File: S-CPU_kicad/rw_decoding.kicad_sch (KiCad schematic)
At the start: 134 parts

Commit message: Schematics tidying in progress.
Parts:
- added GBEG: OR_3, symbol Ricoh_Cells:OR_3
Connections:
- net MODE2_OR_MODE3: now also GBEG.3
- net RW_EN: now also GBEG.4
- net SYNCED_REFRESH_EN: now also GBEG.1
- new net ~{INTERNAL_CYCLE}: GBEG.2
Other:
- company: (none) -> Author: Regis Galland
- title: (none) -> SNES S-CPU Schematics 
- moved on the sheet: AABC, AAFD, BAAG, BABW, BAEH, BAGU, BAIS, BALC, BASL, BATZ, BAUV, CACL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

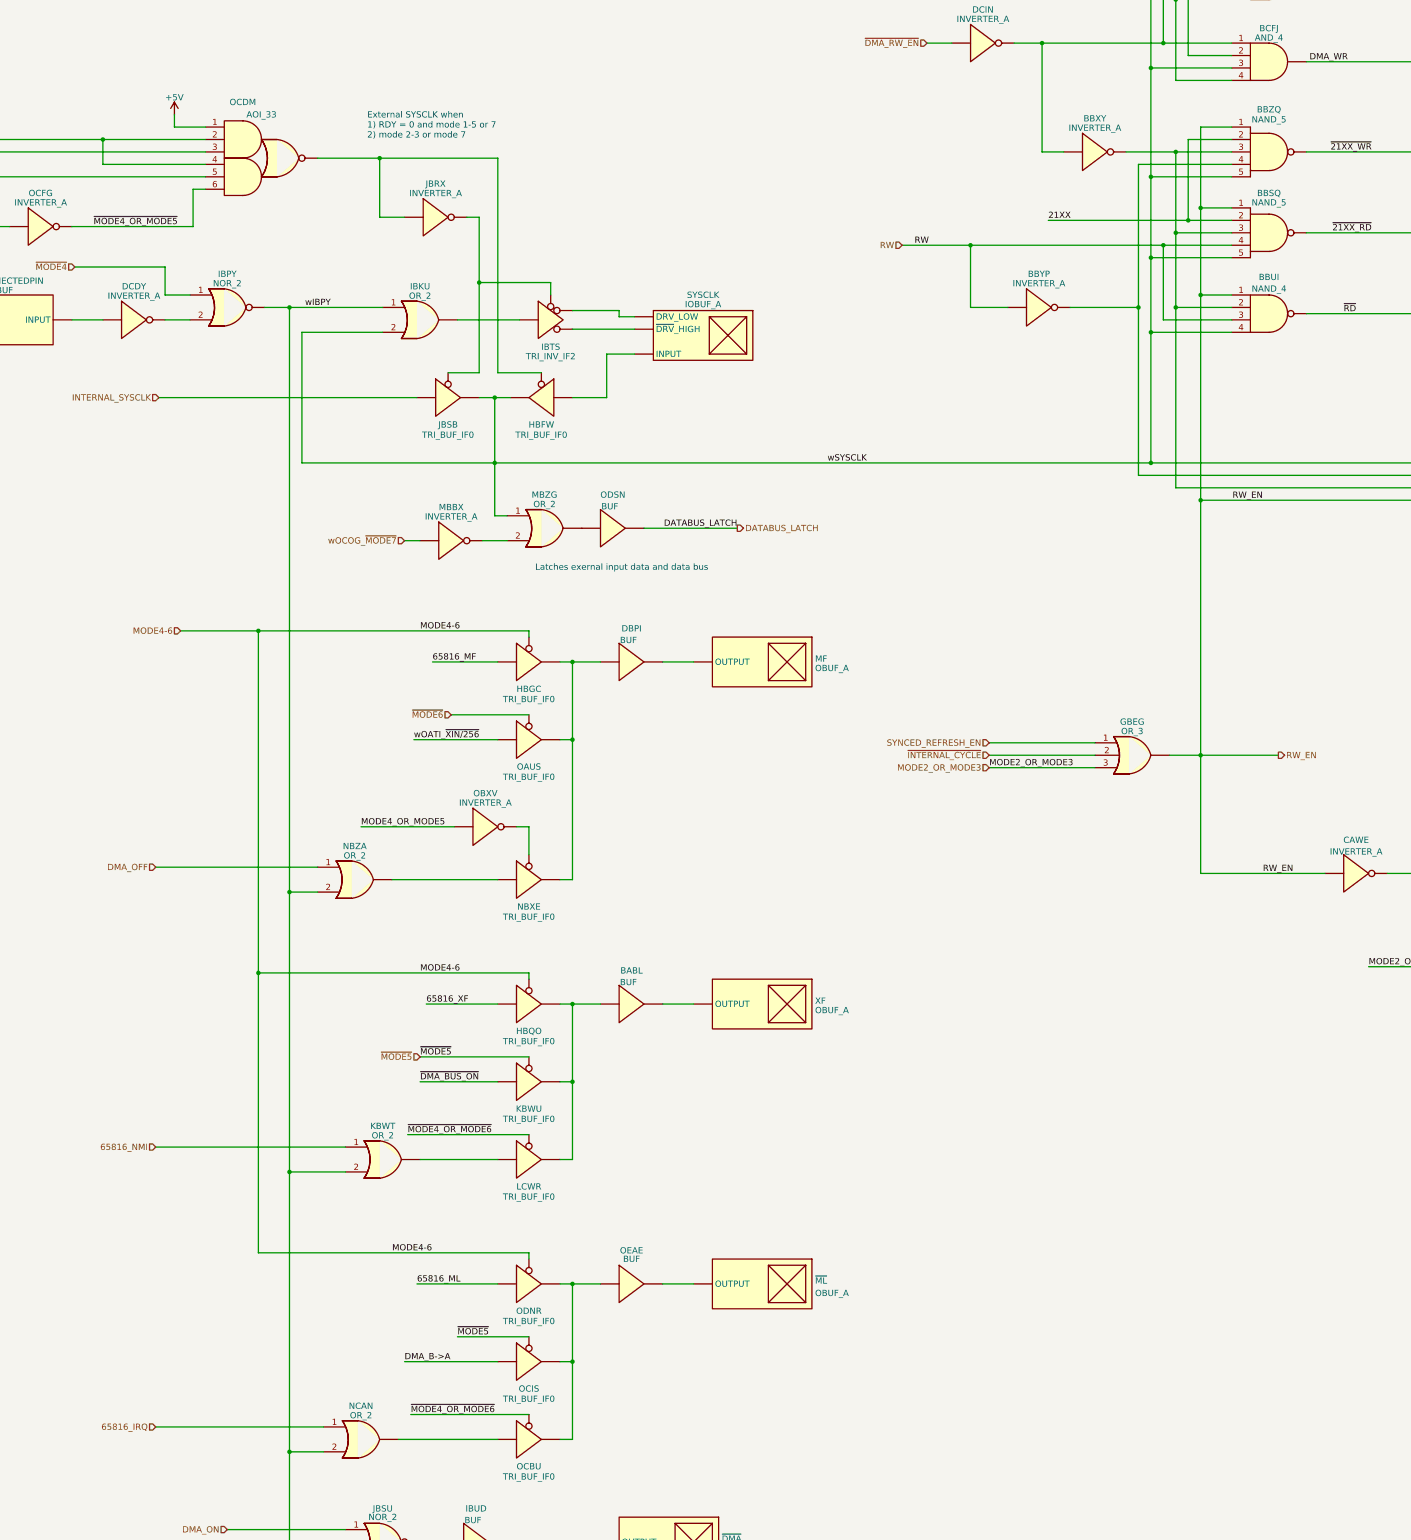
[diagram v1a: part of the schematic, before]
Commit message: Big update on the hierarchical sheet. DMA section update too.
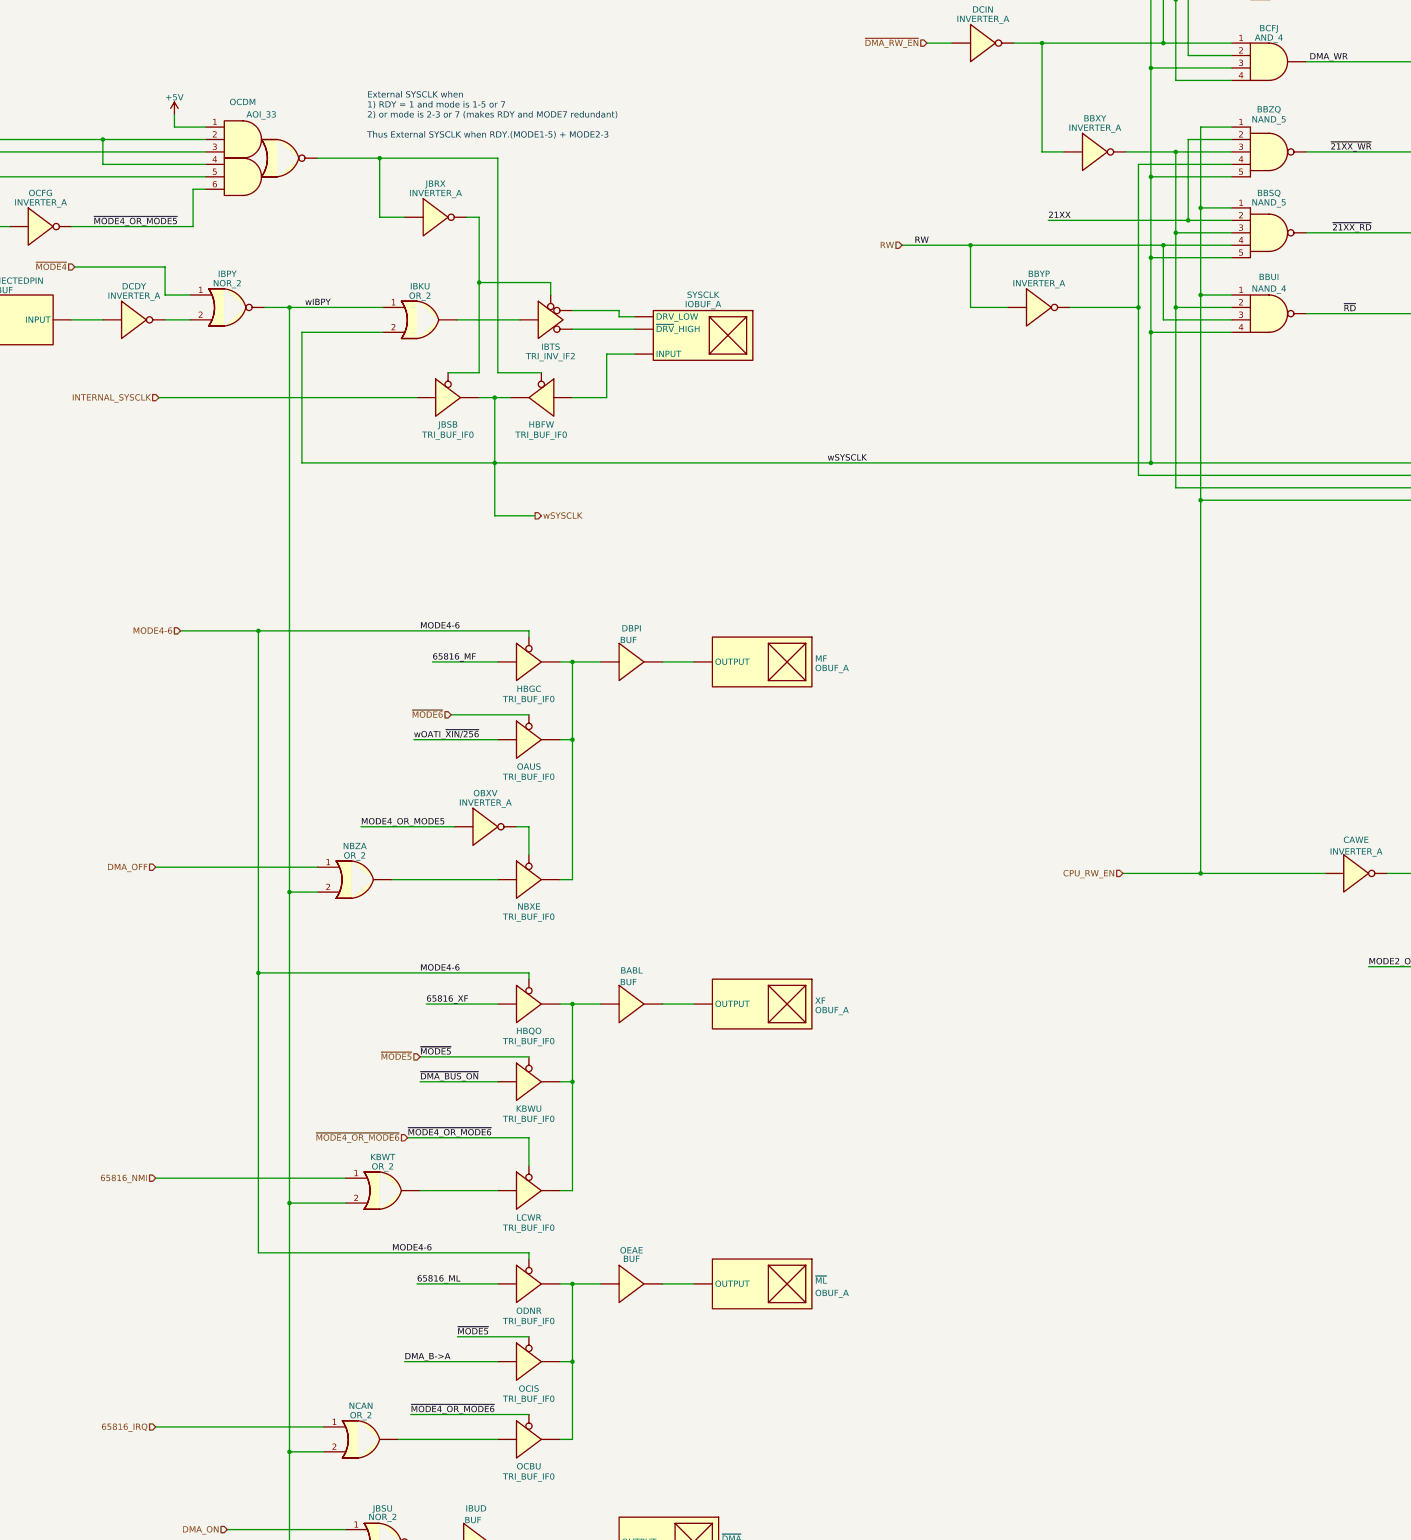
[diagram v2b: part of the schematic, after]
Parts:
- removed GBEG: OR_3, symbol Ricoh_Cells:OR_3
- removed MBBX: INVERTER_A, symbol Ricoh_Cells:INVERTER_A
- removed MBZG: OR_2, symbol Ricoh_Cells:OR_2
- removed ODSN: BUF, symbol Ricoh_Cells:BUF
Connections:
- net RW_EN renamed CPU_RW_EN
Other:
- note added: "External SYSCLK when 1) RDY = 1 and mode is 1-5 or 7 2) or mode is 2-3 or 7 (makes RDY and MODE7 redundant) Thus External SYSCLK when RDY.(MODE1-5) + MODE2-3"
- note removed: "External SYSCLK when 1) RDY = 0 and mode 1-5 or 7 2) mode 2-3 or mode 7"
- note removed: "Latches exernal input data and data bus"
- moved on the sheet: KBWT, LCWR

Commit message: DMA section update. Found errors between some MUX and MUXI gates.
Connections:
- net RW renamed R~{W}
- net ~{DMA_BUS_ON} renamed HDMA_TABLE_RD
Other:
- note added: "Internal registers only In NES mode (MODE2-3), only 4016 and 4017 will set CPU_REG_RD to 1."
- note removed: "Internal registers only"
- moved on the sheet: BBXY, BBYP
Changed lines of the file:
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@@
   (junction (at 533.4 466.725) (diameter 0) (color 0 0 0 0)
   )
-  (junction (at 363.855 187.96) (diameter 0) (color 0 0 0 0)
-  )
   (junction (at 371.475 172.72) (diameter 0) (color 0 0 0 0)
   )
@@
   (junction (at 344.17 133.985) (diameter 0) (color 0 0 0 0)
   )
+  (junction (at 363.855 158.75) (diameter 0) (color 0 0 0 0)
+  )
   (junction (at 229.235 182.88) (diameter 0) (color 0 0 0 0)
   )
@@
   )
   (junction (at 521.335 441.96) (diameter 0) (color 0 0 0 0)
-  )
-  (junction (at 376.555 303.53) (diameter 0) (color 0 0 0 0)
   )
   (no_connect (at 436.245 202.565))
@@
     (stroke (width 0) (type default))
   )
-  (wire (pts (xy 363.855 187.96) (xy 363.855 158.75))
-    (stroke (width 0) (type default))
-  )
   (wire (pts (xy 561.34 330.2) (xy 568.325 330.2))
     (stroke (width 0) (type default))
@@
     (stroke (width 0) (type default))
   )
-  (wire (pts (xy 376.555 303.53) (xy 401.955 303.53))
+  (wire (pts (xy 395.605 303.53) (xy 401.955 303.53))
     (stroke (width 0) (type default))
   )
@@
     (stroke (width 0) (type default))
   )
-  (wire (pts (xy 329.565 187.96) (xy 337.185 187.96))
+  (wire (pts (xy 329.565 158.75) (xy 334.01 158.75))
     (stroke (width 0) (type default))
   )
@@
     (stroke (width 0) (type default))
   )
-  (wire (pts (xy 349.885 187.96) (xy 363.855 187.96))
+  (wire (pts (xy 346.71 158.75) (xy 363.855 158.75))
     (stroke (width 0) (type default))
   )
@@
     (stroke (width 0) (type default))
   )
-  (wire (pts (xy 363.855 187.96) (xy 363.855 222.25))
+  (wire (pts (xy 363.855 158.75) (xy 363.855 222.25))
     (stroke (width 0) (type default))
   )
@@
     (stroke (width 0) (type default))
   )
-  (wire (pts (xy 361.315 156.21) (xy 371.475 156.21))
+  (wire (pts (xy 361.315 146.05) (xy 371.475 146.05))
     (stroke (width 0) (type default))
   )
@@
     (stroke (width 0) (type default))
   )
-  (wire (pts (xy 376.555 227.33) (xy 376.555 303.53))
-    (stroke (width 0) (type default))
-  )
   (wire (pts (xy 532.765 132.715) (xy 530.225 132.715))
     (stroke (width 0) (type default))
@@
     (stroke (width 0) (type default))
   )
-  (wire (pts (xy 344.17 156.21) (xy 344.17 133.985))
+  (wire (pts (xy 344.17 146.05) (xy 344.17 133.985))
     (stroke (width 0) (type default))
   )
@@
     (stroke (width 0) (type default))
   )
+  (wire (pts (xy 371.475 146.05) (xy 371.475 156.21))
+    (stroke (width 0) (type default))
+  )
   (wire (pts (xy 468.63 394.335) (xy 476.25 394.335))
     (stroke (width 0) (type default))
@@
     (stroke (width 0) (type default))
   )
-  (wire (pts (xy 344.17 156.21) (xy 348.615 156.21))
+  (wire (pts (xy 344.17 146.05) (xy 348.615 146.05))
     (stroke (width 0) (type default))
   )
@@
     (stroke (width 0) (type default))
   )
-  (wire (pts (xy 329.565 175.26) (xy 329.565 187.96))
+  (wire (pts (xy 329.565 158.75) (xy 329.565 175.26))
     (stroke (width 0) (type default))
   )
@@
     (stroke (width 0) (type default))
   )
-  (wire (pts (xy 376.555 303.53) (xy 360.68 303.53))
+  (wire (pts (xy 376.555 227.33) (xy 358.775 227.33))
     (stroke (width 0) (type default))
   )
@@
     (effects (font (size 5 5) (thickness 1) bold) (justify left bottom))
   )
-  (text "Internal registers only" (at 631.825 318.77 0)
+  (text "Internal registers only\nIn NES mode (MODE2-3), only 4016 and 4017\nwill set CPU_REG_RD to 1. "
+    (at 617.855 329.565 0)
     (effects (font (size 1.27 1.27)) (justify left bottom))
   )
@@
     (effects (font (size 1.27 1.27)) (justify left bottom))
   )
-  (label "RW" (at 318.135 175.26 0) (fields_autoplaced)
+  (label "R~{W}" (at 318.135 175.26 0) (fields_autoplaced)
     (effects (font (size 1.27 1.27)) (justify left bottom))
   )
@@
     (effects (font (size 1.27 1.27)) (justify left bottom))
   )
-  (label "~{DMA_BUS_ON}" (at 317.5 87.63 0) (fields_autoplaced)
+  (label "HDMA_TABLE_RD" (at 317.5 87.63 0) (fields_autoplaced)
     (effects (font (size 1.27 1.27)) (justify left bottom))
   )
@@
     (effects (font (size 1.27 1.27)) (justify right bottom))
   )
-  (label "~{DMA_BUS_ON}" (at 217.17 346.075 0) (fields_autoplaced)
+  (label "HDMA_TABLE_RD" (at 217.17 346.075 0) (fields_autoplaced)
     (effects (font (size 1.27 1.27)) (justify left bottom))
   )
@@
     (effects (font (size 1.27 1.27)) (justify right))
   )
+  (hierarchical_label "CPU_RW_EN" (shape input) (at 395.605 303.53 180) (fields_autoplaced)
+    (effects (font (size 1.27 1.27)) (justify right))
+  )
   (hierarchical_label "~{MODE1}" (shape input) (at 128.27 161.29 180) (fields_autoplaced)
     (effects (font (size 1.27 1.27)) (justify right))
@@
     (effects (font (size 1.27 1.27)) (justify right))
   )
-  (hierarchical_label "RW" (shape input) (at 315.595 175.26 180) (fields_autoplaced)
+  (hierarchical_label "R~{W}" (shape input) (at 315.595 175.26 180) (fields_autoplaced)
     (effects (font (size 1.27 1.27)) (justify right))
   )
@@
     (effects (font (size 1.27 1.27)) (justify right))
   )
-  (hierarchical_label "CPU_RW_EN" (shape input) (at 360.68 303.53 180) (fields_autoplaced)
+  (hierarchical_label "CPU_RW_EN" (shape input) (at 358.775 227.33 180) (fields_autoplaced)
     (effects (font (size 1.27 1.27)) (justify right))
   )
@@
     (effects (font (size 1.27 1.27)) (justify left))
   )
-  (hierarchical_label "~{DMA_BUS_ON}" (shape input) (at 317.5 87.63 180) (fields_autoplaced)
+  (hierarchical_label "HDMA_TABLE_RD" (shape input) (at 317.5 87.63 180) (fields_autoplaced)
     (effects (font (size 1.27 1.27)) (justify right))
   )
@@
     )
   )
-  (symbol (lib_id "Ricoh_Cells:INVERTER_A") (at 354.965 156.21 0) (unit 1)
+  (symbol (lib_id "Ricoh_Cells:INVERTER_A") (at 354.965 146.05 0) (unit 1)
     (in_bom yes) (on_board yes) (dnp no) (fields_autoplaced)
-    (property "Reference" "BBXY" (at 354.965 149.3901 0)
-      (effects (font (size 1.27 1.27)))
-    )
-    (property "Value" "INVERTER_A" (at 354.965 151.3111 0)
-      (effects (font (size 1.27 1.27)))
-    )
-    (property "Footprint" "" (at 352.425 156.21 0)
-      (effects (font (size 1.27 1.27)) hide)
-    )
-    (property "Datasheet" "http://iceboy.a-singer.de/doc/dmg_cells.html#inv_a" (at 356.235 163.83 0)
+    (property "Reference" "BBXY" (at 354.965 139.2301 0)
+      (effects (font (size 1.27 1.27)))
+    )
+    (property "Value" "INVERTER_A" (at 354.965 141.1511 0)
+      (effects (font (size 1.27 1.27)))
+    )
+    (property "Footprint" "" (at 352.425 146.05 0)
+      (effects (font (size 1.27 1.27)) hide)
+    )
+    (property "Datasheet" "http://iceboy.a-singer.de/doc/dmg_cells.html#inv_a" (at 356.235 153.67 0)
       (effects (font (size 1.27 1.27)) hide)
     )
@@
     )
   )
-  (symbol (lib_id "Ricoh_Cells:INVERTER_A") (at 343.535 187.96 0) (unit 1)
+  (symbol (lib_id "Ricoh_Cells:INVERTER_A") (at 340.36 158.75 0) (unit 1)
     (in_bom yes) (on_board yes) (dnp no) (fields_autoplaced)
-    (property "Reference" "BBYP" (at 343.535 181.1401 0)
-      (effects (font (size 1.27 1.27)))
-    )
-    (property "Value" "INVERTER_A" (at 343.535 183.0611 0)
-      (effects (font (size 1.27 1.27)))
-    )
-    (property "Footprint" "" (at 340.995 187.96 0)
-      (effects (font (size 1.27 1.27)) hide)
-    )
-    (property "Datasheet" "http://iceboy.a-singer.de/doc/dmg_cells.html#inv_a" (at 344.805 195.58 0)
-      (effects (font (size 1.27 1.27)) hide)
-    )
+    (property "Reference" "BBYP" (at 340.36 151.9301 0)
+      (effects (font (size 1.27 1.27)))
+    )
+    (property "Value" "INVERTER_A" (at 340.36 153.8511 0)
+      (effects (font (size 1.27 1.27)))
+    )
+    (property "Footprint" "" (at 337.82 158.75 0)
+      (effects (font (size 1.27 1.27)) hide)
+    )
+    (property "Datasheet" "http://iceboy.a-singer.de/doc/dmg_cells.html#inv_a" (at 341.63 166.37 0)
+      (effects (font (size 1.27 1.27)) hide)
+    )
